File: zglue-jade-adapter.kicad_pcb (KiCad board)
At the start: 8 copper layers, 25 x 20 mm, 63 parts, among them J1 543630489, J2 543630489, U1 zGlue-Jade

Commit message: Add initial layout
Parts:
- added TP32: TP_SMD1MM, antmicro-footprints:Testpoint_smd_1mm, F.Cu at (17.2, 15.6)
- added TP33: TP_SMD1MM, antmicro-footprints:Testpoint_smd_1mm, F.Cu at (0.76, 19.2)
- added TP34: TP_SMD1MM, antmicro-footprints:Testpoint_smd_1mm, F.Cu at (18.8, 4.62)
- C11: value C_100n_0402_6V3 -> C_1u_0603; footprint antmicro-footprints:0402-cap -> antmicro-footprints:0603-cap
- moved TP14 20.3 mm to (0.69, 3.45), turned to 0 degrees
- moved TP16 20.0 mm to (0.97, 6.31), turned to 0 degrees
- moved TP15 16.9 mm to (1.06, 9.64), turned to 0 degrees
- moved R3 13.8 mm to (19.2, 9.64)
- moved C3 11.9 mm to (14.2, 17.2), turned to 270 degrees
- moved C7 11.9 mm to (18.3, 9.63)
- moved C1 10.5 mm to (7.91, 13.8), turned to 270 degrees
- moved C2 7.45 mm to (11.4, 16.8)
- moved R5 4.68 mm to (14.8, 19.1), turned to 0 degrees
- moved R2 4.57 mm to (16.5, 17.4), turned to 90 degrees
- moved C9 3.08 mm to (7.37, 11.7), turned to 270 degrees
- moved C6 2.34 mm to (17.8, 11.5), turned to 90 degrees
- moved C11 2.08 mm to (6.41, 13.6)
- moved C5 2.05 mm to (17.8, 13.6), turned to 270 degrees
- moved R7 2.05 mm to (4.99, 15.0)
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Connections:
- C1 pad 1: /3V3_SYS -> /3V3
- C2 pad 1: /1V8_SYS -> /1V8
- C3 pad 1: /2V5_SYS -> /2V5
- C4 pad 1: /1V2_SYS -> /1V2
- R4 pad 2: /1V2_SYS -> Net-(R4-Pad2)
- R5 pad 1: /1V2_SYS -> Net-(R4-Pad2)
- U1 pad L10: /3V3_SYS -> /1V8_SYS
- U1 pad M10: /1V8_SYS -> /3V3_SYS
- U1 pad N1: /VDDIO_BST -> /BOOST_OUT
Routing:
- net /3V3_SYS: track 0.69 -> 54.2 mm, vias 0 -> 3
- net GND: track 2.51 -> 52.1 mm, vias 0 -> 27
- net /2V5_SYS: track 0.00 -> 36.8 mm, vias 0 -> 1
- net /1V8_SYS: track 0.00 -> 34.7 mm, vias 0 -> 3
- net /I2C_0_SDA: track 0.00 -> 31.6 mm, vias 0 -> 2
- net /I2C_0_SCL: track 0.00 -> 31.5 mm, vias 0 -> 2
- net /1V2_SYS: track 0.00 -> 31.3 mm, vias 0 -> 1
- net /USB_D_P: track 0.00 -> 31.1 mm, vias 0 -> 3
- net /USB_D_N: track 0.00 -> 30.7 mm, vias 0 -> 3
- net /PIO16: track 2.17 -> 32.2 mm, vias 0 -> 3
- net /USB_DET: track 0.00 -> 29.7 mm, vias 0 -> 4
- net /DONE: track 1.38 -> 29.6 mm, vias 1 -> 3
- net /FLASH_IO3: track 0.00 -> 28.2 mm, vias 0 -> 1
- net /FLASH_IO2: track 0.00 -> 27.6 mm, vias 0 -> 1
- net /FLASH_IO0: track 0.00 -> 27.4 mm, vias 0 -> 1
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- added copper zone on Ground_Layer2, net GND
- added copper zone on Ground_layer1, net GND
- removed copper zone on Power_Layer2, net /1V2_SYS
- removed copper zone on Power_Layer1, net /3V3_SYS
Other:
- copper layers 8 -> 6
- net class Default: via_dia 0.4 -> 0.457; via_drill 0.1 -> 0.2
- rule via_min_size: 0.4 -> 0.457
- board text added: "Rev. 1.0 10/2019"

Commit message: Tune differential pairs
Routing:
- net /CSI_D2_IN_N: track 18.8 -> 23.4 mm
- net /CSI_CLK_IN_N: track 19.1 -> 23.4 mm
- net /CSI_CLK_IN_P: track 19.6 -> 23.4 mm
- net /CSI_D2_IN_P: track 20.5 -> 23.3 mm
- net /CSI_D1_IN_P: track 21.1 -> 23.4 mm
- net GND: track 52.1 -> 53.2 mm
- net /CSI_D1_OUT_P: track 12.5 -> 13.4 mm
- net /CSI_D1_OUT_N: track 12.8 -> 13.8 mm
- net /USB_D_P: track 31.1 -> 31.9 mm
- net /CSI_CLK_OUT_N: track 13.2 -> 13.9 mm
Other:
- board text added: "0.02mm"
- board text added: "0.035mm"
- board text added: "0.12"
- board text added: "0.12mm"
- board text added: "0.14"
- board text added: "0.2"
- board text added: "1"
- board text added: "3.5"
- board text added: "4.2"
- board text added: "Bottom Layer"
- board text added: "Bottom Solder"
- board text added: "Constant"
- board text added: "Copper"
- board text added: "Core 1"
- board text added: "Core 2"
- board text added: "Dielectric 1"
- board text added: "Dielectric 3"
- board text added: "Dielectric2"
- board text added: "FR-4"
- board text added: "Ground Plane 1"
- board text added: "Ground Plane 2"
- board text added: "Layer"
- board text added: "Material"
- board text added: "Name"
- board text added: "Signal Layer 1"
- board text added: "Signal Layer 2"
- board text added: "Solder Resist"
- board text added: "Thickness"
- board text added: "Top Layer"
- board text added: "Top Solder"

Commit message: Minor tweaks
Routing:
- net /3V3_SYS: track 54.2 -> 59.8 mm
- net /2V5_SYS: track 36.8 -> 36.2 mm
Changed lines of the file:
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@@
   (via (at 18.27 18.65) (size 0.457) (drill 0.2) (layers Top_Layer Bottom_Layer) (net 9))
   (segment (start 18.27 15.03) (end 18.27 18.65) (width 0.2) (layer Top_Layer) (net 9))
-  (segment (start 2.027 14.757) (end 2.82 15.55) (width 0.15) (layer Bottom_Layer) (net 9))
-  (segment (start 2.82 15.55) (end 2.82 18.49) (width 0.15) (layer Bottom_Layer) (net 9))
-  (segment (start 2.82 18.49) (end 4.06 19.73) (width 0.15) (layer Bottom_Layer) (net 9))
-  (segment (start 17.19 19.73) (end 18.27 18.65) (width 0.15) (layer Bottom_Layer) (net 9))
-  (segment (start 4.06 19.73) (end 17.19 19.73) (width 0.15) (layer Bottom_Layer) (net 9))
   (segment (start 8.99 5.312) (end 8.99 5.1) (width 0.2) (layer Top_Layer) (net 9))
   (segment (start 8.99 5.1) (end 6.93 3.04) (width 0.2) (layer Top_Layer) (net 9))
   (segment (start 6.93 3.04) (end 4.38 3.04) (width 0.2) (layer Top_Layer) (net 9))
   (via (at 4.38 3.04) (size 0.457) (drill 0.2) (layers Top_Layer Bottom_Layer) (net 9))
-  (via (at 1.91 14.757) (size 0.457) (drill 0.2) (layers Top_Layer Bottom_Layer) (net 9))
-  (segment (start 1.00212 14.757) (end 1.91 14.757) (width 0.15) (layer Bottom_Layer) (net 9))
-  (segment (start 1.91 14.757) (end 2.027 14.757) (width 0.15) (layer Bottom_Layer) (net 9))
-  (segment (start 1.827 14.84) (end 1.91 14.757) (width 0.1) (layer Signal_Layer2) (net 9))
-  (segment (start 1.06 13.907) (end 1.91 14.757) (width 0.2) (layer Signal_Layer2) (net 9))
-  (segment (start 1.06 6.036853) (end 1.06 13.907) (width 0.2) (layer Signal_Layer2) (net 9))
   (segment (start 4.056853 3.04) (end 1.06 6.036853) (width 0.2) (layer Signal_Layer2) (net 9))
   (segment (start 4.38 3.04) (end 4.056853 3.04) (width 0.2) (layer Signal_Layer2) (net 9))
+  (segment (start 0.60212 14.757) (end 0.26 15.09912) (width 0.2) (layer Bottom_Layer) (net 9))
+  (segment (start 1.00212 14.757) (end 0.60212 14.757) (width 0.2) (layer Bottom_Layer) (net 9))
+  (segment (start 0.26 15.09912) (end 0.26 16.9) (width 0.2) (layer Bottom_Layer) (net 9))
+  (via (at 0.56 17.2) (size 0.457) (drill 0.2) (layers Top_Layer Bottom_Layer) (net 9))
+  (segment (start 0.26 16.9) (end 0.56 17.2) (width 0.2) (layer Bottom_Layer) (net 9))
+  (segment (start 1.06 16.7) (end 0.56 17.2) (width 0.2) (layer Signal_Layer2) (net 9))
+  (segment (start 1.06 13.65) (end 1.06 16.7) (width 0.2) (layer Signal_Layer2) (net 9))
+  (segment (start 1.06 6.036853) (end 1.06 13.65) (width 0.2) (layer Signal_Layer2) (net 9))
+  (segment (start 1.06 13.65) (end 1.06 13.907) (width 0.2) (layer Signal_Layer2) (net 9))
+  (segment (start 2.027 14.757) (end 2.82 15.55) (width 0.2) (layer Bottom_Layer) (net 9))
+  (segment (start 1.00212 14.757) (end 2.027 14.757) (width 0.2) (layer Bottom_Layer) (net 9))
+  (segment (start 2.82 18.49) (end 4.06 19.73) (width 0.2) (layer Bottom_Layer) (net 9))
+  (segment (start 2.82 15.55) (end 2.82 18.49) (width 0.2) (layer Bottom_Layer) (net 9))
+  (segment (start 17.19 19.73) (end 18.27 18.65) (width 0.2) (layer Bottom_Layer) (net 9))
+  (segment (start 4.06 19.73) (end 17.19 19.73) (width 0.2) (layer Bottom_Layer) (net 9))
   (segment (start 10.87 13.58) (end 10.865 13.58) (width 0.15) (layer Top_Layer) (net 11))
   (segment (start 10.865 13.58) (end 10.52 13.925) (width 0.15) (layer Top_Layer) (net 11))
@@
   (segment (start 19.66 16.908537) (end 19.694963 16.9435) (width 0.15) (layer Top_Layer) (net 25))
   (segment (start 19.27001 16.51001) (end 19.694963 16.9435) (width 0.15) (layer Top_Layer) (net 25))
-  (segment (start 19.694963 16.9435) (end 19.694963 18.035037) (width 0.15) (layer Signal_Layer2) (net 25))
-  (segment (start 18.141499 19.588501) (end 15.758501 19.588501) (width 0.15) (layer Signal_Layer2) (net 25))
-  (segment (start 19.694963 18.035037) (end 18.141499 19.588501) (width 0.15) (layer Signal_Layer2) (net 25))
   (segment (start 6.976221 13.810779) (end 6.976221 14.84372) (width 0.15) (layer Top_Layer) (net 25))
   (segment (start 7.487 13.3) (end 6.976221 13.810779) (width 0.15) (layer Top_Layer) (net 25))
@@
   (via (at 7.276762 15.99251) (size 0.457) (drill 0.2) (layers Top_Layer Bottom_Layer) (net 25))
   (segment (start 6.923117 15.713117) (end 7.20251 15.99251) (width 0.15) (layer Top_Layer) (net 25))
-  (segment (start 8.16 19.588501) (end 7.968501 19.588501) (width 0.15) (layer Signal_Layer2) (net 25))
-  (segment (start 15.758501 19.588501) (end 8.16 19.588501) (width 0.15) (layer Signal_Layer2) (net 25))
-  (segment (start 7.46 19.08) (end 7.46 19.0165) (width 0.15) (layer Signal_Layer2) (net 25))
-  (via (at 7.46 19.0165) (size 0.457) (drill 0.2) (layers Top_Layer Bottom_Layer) (net 25))
-  (segment (start 7.968501 19.588501) (end 7.46 19.08) (width 0.15) (layer Signal_Layer2) (net 25))
-  (segment (start 7.276762 18.833262) (end 7.46 19.0165) (width 0.15) (layer Signal_Layer1) (net 25))
-  (segment (start 7.276762 15.99251) (end 7.276762 18.833262) (width 0.15) (layer Signal_Layer1) (net 25))
+  (segment (start 7.688499 19.224989) (end 7.46 18.99649) (width 0.15) (layer Signal_Layer2) (net 25))
+  (segment (start 7.276762 15.99251) (end 7.276762 18.813252) (width 0.15) (layer Signal_Layer1) (net 25))
+  (via (at 7.46 18.99649) (size 0.457) (drill 0.2) (layers Top_Layer Bottom_Layer) (net 25))
+  (segment (start 8.052011 19.588501) (end 7.688499 19.224989) (width 0.15) (layer Signal_Layer2) (net 25))
+  (segment (start 7.276762 18.813252) (end 7.46 18.99649) (width 0.15) (layer Signal_Layer1) (net 25))
+  (segment (start 19.694963 18.035037) (end 18.141499 19.588501) (width 0.15) (layer Signal_Layer2) (net 25))
+  (segment (start 19.694963 16.9435) (end 19.694963 18.035037) (width 0.15) (layer Signal_Layer2) (net 25))
+  (segment (start 18.141499 19.588501) (end 8.052011 19.588501) (width 0.15) (layer Signal_Layer2) (net 25))
   (via (at 16.341 11.837) (size 0.457) (drill 0.2) (layers Top_Layer Bottom_Layer) (net 26))
   (segment (start 16.215 11.837) (end 16.341 11.837) (width 0.1) (layer Top_Layer) (net 26))
@@
   (segment (start 3.16 15.13) (end 3.16 18.32) (width 0.2) (layer Bottom_Layer) (net 50))
   (segment (start 2.287 14.257) (end 3.16 15.13) (width 0.2) (layer Bottom_Layer) (net 50))
-  (segment (start 3.97 19.13) (end 4.31999 19.47999) (width 0.2) (layer Bottom_Layer) (net 50))
   (segment (start 3.16 18.32) (end 3.97 19.13) (width 0.2) (layer Bottom_Layer) (net 50))
-  (segment (start 3.97 19.13) (end 4.31 19.47) (width 0.2) (layer Bottom_Layer) (net 50))
-  (segment (start 4.31999 19.47999) (end 10.00001 19.47999) (width 0.2) (layer Bottom_Layer) (net 50))
-  (segment (start 10.00001 19.47999) (end 16.73001 19.47999) (width 0.2) (layer Bottom_Layer) (net 50))
   (via (at 17 19.21) (size 0.457) (drill 0.2) (layers Top_Layer Bottom_Layer) (net 50))
-  (segment (start 16.73001 19.47999) (end 17 19.21) (width 0.2) (layer Bottom_Layer) (net 50))
   (segment (start 18.76 19.21) (end 17 19.21) (width 0.2) (layer Top_Layer) (net 50))
   (segment (start 20.115501 17.854499) (end 18.76 19.21) (width 0.2) (layer Top_Layer) (net 50))
   (segment (start 20.115501 10.712501) (end 20.115501 17.854499) (width 0.2) (layer Top_Layer) (net 50))
   (segment (start 19.522 10.119) (end 20.115501 10.712501) (width 0.2) (layer Top_Layer) (net 50))
+  (segment (start 16.81 19.4) (end 17 19.21) (width 0.2) (layer Bottom_Layer) (net 50))
+  (segment (start 4.24 19.4) (end 16.81 19.4) (width 0.2) (layer Bottom_Layer) (net 50))
+  (segment (start 3.97 19.13) (end 4.24 19.4) (width 0.2) (layer Bottom_Layer) (net 50))
   (via (at 16.99548 7.749122) (size 0.457) (drill 0.2) (layers Top_Layer Bottom_Layer) (net 52))
   (segment (start 5.676219 13.757) (end 5.531219 13.612) (width 0.11) (layer Bottom_Layer) (net 52))

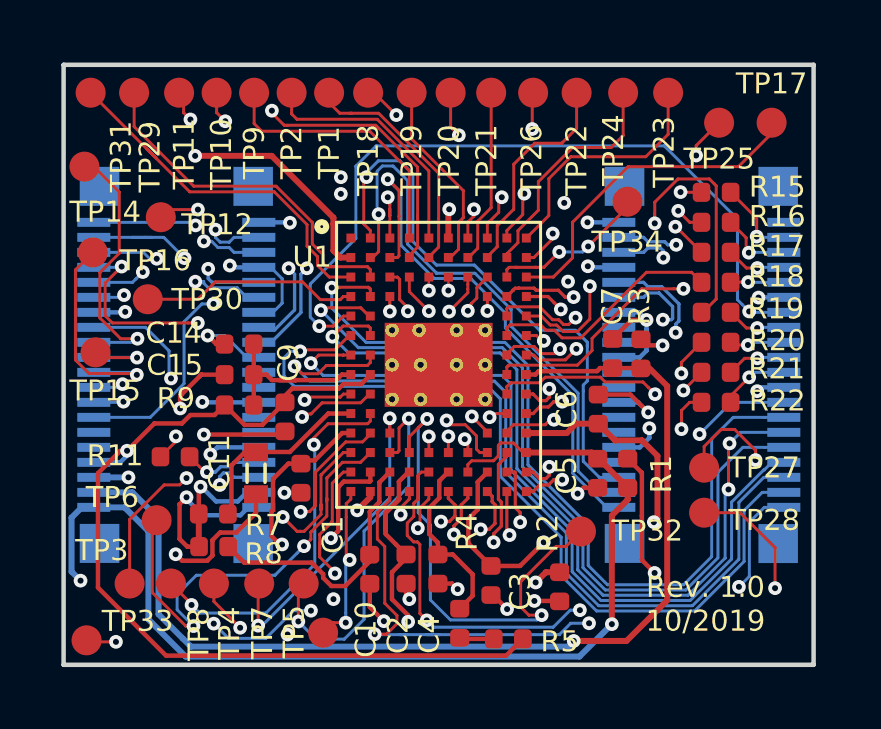
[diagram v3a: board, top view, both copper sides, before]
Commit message: Add CSI_LP and CSI_INT signals and corresponding resistors
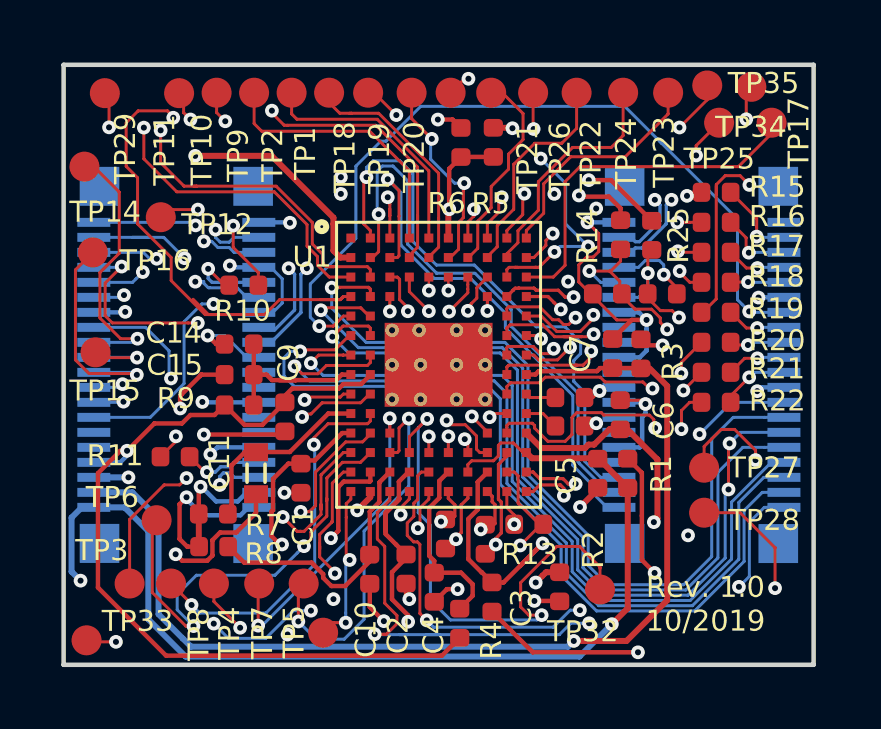
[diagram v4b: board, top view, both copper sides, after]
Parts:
- removed TP30, TP31: TP_SMD1MM, antmicro-footprints:Testpoint_smd_1mm
- added R10: R_220R_0402, antmicro-footprints:0402-res, F.Cu at (6.00, 7.35)
- added R12: R_100R_0402, antmicro-footprints:0402-res, F.Cu at (12.7, 15.6)
- added R13: R_100R_0402, antmicro-footprints:0402-res, F.Cu at (15.5, 15.3)
- added R14: R_22R_0402, antmicro-footprints:0402-res, F.Cu at (18.6, 5.67)
- added R23: R_120R_0402, antmicro-footprints:0402-res, F.Cu at (16.9, 11.1)
- added R24: R_120R_0402, antmicro-footprints:0402-res, F.Cu at (16.9, 12.0)
- added R25: R_22R_0402, antmicro-footprints:0402-res, F.Cu at (19.6, 5.69)
- added R26: R_49R9_0402, antmicro-footprints:0402-res, F.Cu at (18.1, 7.64)
- added R27: R_49R9_0402, antmicro-footprints:0402-res, F.Cu at (19.9, 7.64)
- added R28: R_100R_0402, antmicro-footprints:0402-res, F.Cu at (14.1, 15.8)
- added R6: R_0R_0402, antmicro-footprints:0402-res, F.Cu at (13.2, 2.60)
- added TP35: TP_SMD1MM, antmicro-footprints:Testpoint_smd_1mm, F.Cu at (21.4, 0.74)
- moved R5 16.6 mm to (14.3, 2.59), turned to 270 degrees
- moved TP34 5.63 mm to (22.9, 0.79)
- moved TP32 2.04 mm to (17.9, 17.5)
- moved TP29 0.93 mm to (1.37, 1.00), turned to 0 degrees
- moved C6 0.76 mm to (18.6, 11.7)
- moved C4 0.62 mm to (12.3, 17.4)
- moved C3 0.55 mm to (14.3, 17.7)
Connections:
- net /PIO13 renamed /PROC_INT
- net /PIO14 renamed /CSI_INT
- J2 pad 25: /CSI_D1_OUT_P -> /C_CSI_D1_OUT_P
- J2 pad 26: /CSI_D1_OUT_N -> /C_CSI_D1_OUT_N
- R4 pad 2: Net-(R4-Pad2) -> /1V2_SYS
- R5 pad 1: Net-(R4-Pad2) -> /1V8_SYS
- R5 pad 2: /1V2_SYS -> /RAVEN_VCC
- U1 pad C1: /PIO19 -> /LP_CSI_D1_OUT_N
- U1 pad D1: /PIO18 -> /LP_CSI_D1_OUT_P
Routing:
- net /LP_CSI_D1_OUT_P: track 0.00 -> 34.2 mm, vias 0 -> 2
- net /LP_CSI_D1_OUT_N: track 0.00 -> 30.0 mm, vias 0 -> 2
- net /1V8_SYS: track 34.7 -> 63.1 mm, vias 3 -> 5
- net /CSI_INT: track 9.89 -> 23.0 mm, vias 2 -> 3
- net /CSI_D1_OUT_N: track 13.8 -> 1.14 mm, vias 2 -> 0
- net /CSI_D1_OUT_P: track 13.4 -> 1.02 mm, vias 2 -> 0
- net /PIO19: track 12.2 -> 0.00 mm
- net GND: track 53.2 -> 64.9 mm, vias 27 -> 26
- net /C_CSI_D1_OUT_P: track 0.00 -> 11.0 mm, vias 0 -> 3
- net /3V3_SYS: track 59.8 -> 70.1 mm, vias 3 -> 4
- net Net-(TP34-Pad1): track 6.08 -> 16.4 mm, vias 2 -> 4
- net /C_CSI_D1_OUT_N: track 0.00 -> 10.2 mm, vias 0 -> 3
- net /TDI: track 22.3 -> 31.4 mm
- net Net-(TP35-Pad1): track 1.72 -> 9.59 mm, vias 1 -> 2
- net /PIO18: track 7.30 -> 0.00 mm
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
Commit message: Tune differential pairs
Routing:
- net /C_CSI_D1_OUT_N: track 10.2 -> 13.7 mm
- net /C_CSI_D1_OUT_P: track 11.0 -> 13.5 mm
- net /PROC_SO: track 22.8 -> 23.4 mm
- net /PROC_SI: track 25.6 -> 26.2 mm

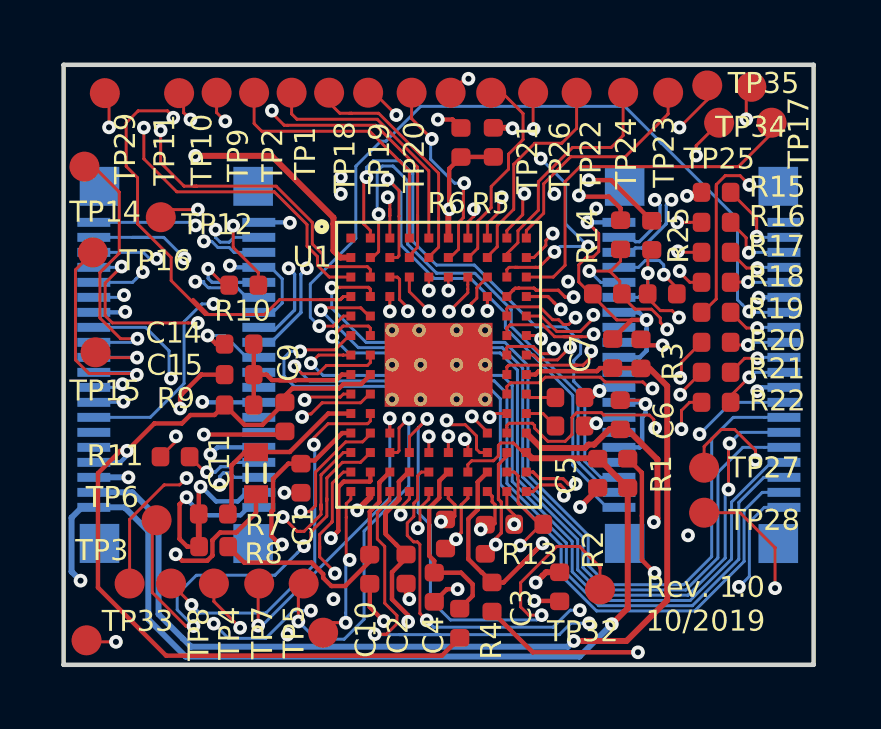
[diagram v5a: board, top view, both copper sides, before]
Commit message: Update pinout and layout
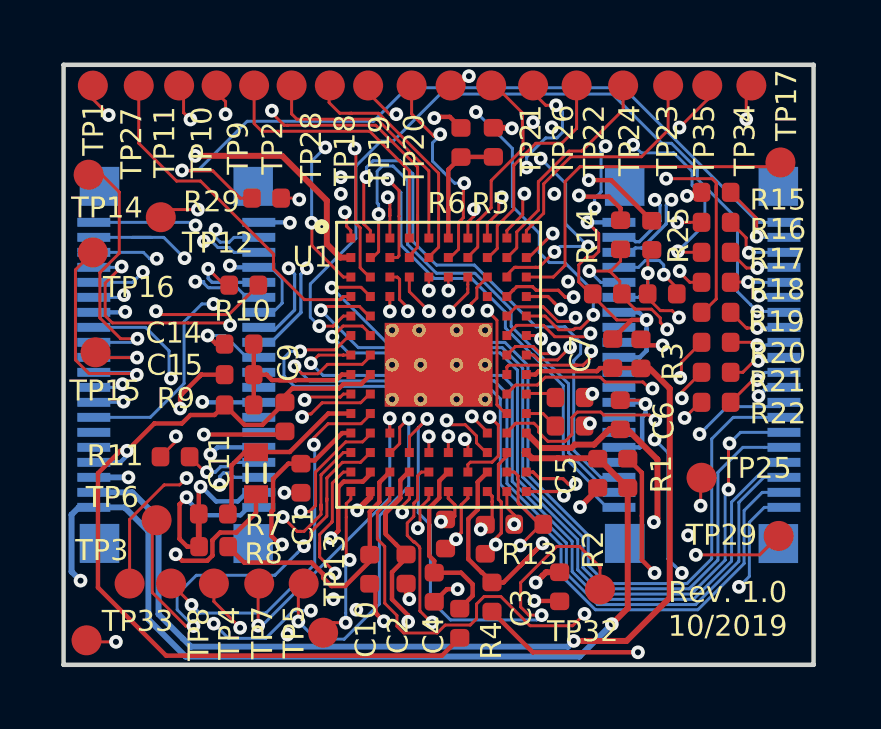
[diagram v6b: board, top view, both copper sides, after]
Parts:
- added R29: R_0R_0402, antmicro-footprints:0402-res, F.Cu at (6.76, 4.45)
- moved TP29 26.9 mm to (23.8, 15.8)
- moved TP27 22.7 mm to (2.45, 0.70)
- moved TP28 18.9 mm to (8.87, 0.74), turned to 0 degrees
- moved TP25 11.8 mm to (21.2, 13.8)
- moved TP1 7.88 mm to (0.97, 0.65)
- moved TP17 1.36 mm to (23.9, 3.21)
- moved TP14 0.30 mm to (0.83, 3.72)
- moved TP11 0.26 mm to (3.85, 0.64)
- moved TP10 0.24 mm to (5.09, 0.64)
- moved TP18 0.24 mm to (10.1, 0.69)
- moved TP19 0.24 mm to (11.5, 0.69)
- moved TP2 0.24 mm to (7.59, 0.64)
- moved TP20 0.24 mm to (12.8, 0.69)
- moved TP21 0.24 mm to (14.2, 0.69)
- moved TP22 0.24 mm to (17.0, 0.69)
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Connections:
- TP1 pad 1: /PIO4 -> /PIO0
- TP25 pad 1: /PROC_INT -> /PIO13
- TP26 pad 1: /CSI_INT -> /PIO14
- TP28 pad 1: /PIO16 -> /PIO4
- TP29 pad 1: /PIO17 -> /PROC_INT
- U1 pad C1: /LP_CSI_D1_OUT_N -> /PROC_SCK
- U1 pad C2: /PIO17 -> /PROC_SS
- U1 pad C3: Net-(U1-PadC3) -> /PIO0
- U1 pad C7: /CSI_INT -> /PROC_SO
- U1 pad C8: /PROC_INT -> /PROC_SI
- U1 pad D1: /LP_CSI_D1_OUT_P -> /PIO15
- U1 pad E10: /PIO15 -> /PIO13
- U1 pad F10: /PROC_SCK -> /CTRL_SCK
- U1 pad F9: /PROC_SS -> /CTRL_SS
- U1 pad G9: /PIO16 -> /PIO14
- U1 pad N5: /CTRL_SCK -> /LP_CSI_D1_OUT_N
- U1 pad P3: /CTRL_SS -> /PROC_INT
- U1 pad P4: /PROC_SI -> /CSI_INT
- U1 pad P5: /PROC_SO -> /LP_CSI_D1_OUT_P
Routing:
- net /PIO13: track 0.00 -> 36.2 mm, vias 0 -> 3
- net /PIO16: track 32.5 -> 0.00 mm, vias 3 -> 0
- net /E_PROC_RST: track 0.00 -> 25.8 mm, vias 0 -> 1
- net /PIO0: track 0.00 -> 17.1 mm, vias 0 -> 2
- net /3V3_SYS: track 70.1 -> 84.3 mm, vias 4 -> 7
- net /PIO17: track 13.9 -> 0.00 mm, vias 2 -> 0
- net /PIO14: track 0.00 -> 13.1 mm, vias 0 -> 4
- net /PROC_SCK: track 9.55 -> 22.4 mm, vias 2 -> 4
- net /PIO15: track 23.9 -> 11.4 mm, vias 2 -> 0
- net /PROC_SS: track 9.52 -> 19.8 mm, vias 2 -> 4
- net /CTRL_SS: track 23.0 -> 13.9 mm, vias 3 -> 2
- net /LP_CSI_D1_OUT_P: track 34.2 -> 26.5 mm
- net /CTRL_SCK: track 20.9 -> 13.9 mm, vias 3 -> 2
- net /PROC_INT: track 13.8 -> 20.2 mm
- net /PROC_SI: track 26.2 -> 20.1 mm, vias 2 -> 3
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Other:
- board text added: "TP13"
